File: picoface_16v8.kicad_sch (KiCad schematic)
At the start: 23 parts, among them J1 ZX_Spectrum_Connector_48K_SOR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, J2 DE9_Plug, Q1 DMG2305, SW1 SW_USER, SW2 SW_RESET, SW3 SW_RUN, U2 Pico, U3 74LS240

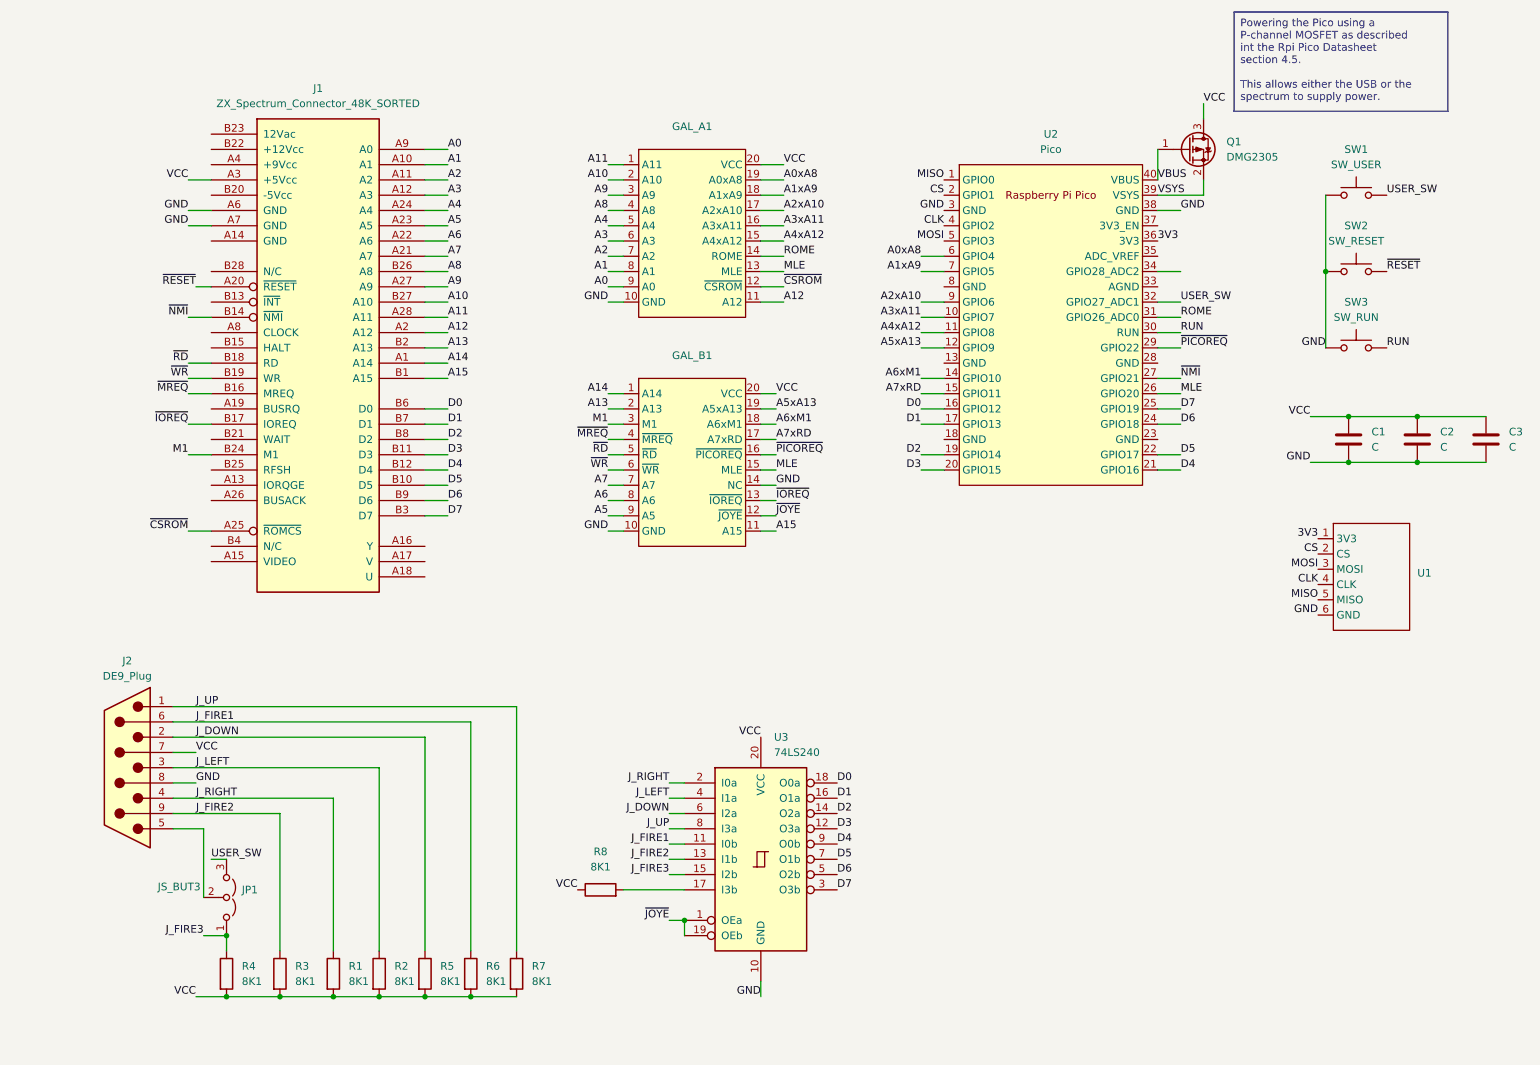
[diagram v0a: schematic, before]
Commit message: Correct resistor typo and add GALASM to schematic
I just blindly typed in 8K1 whereas the resistor I have are 8K2.
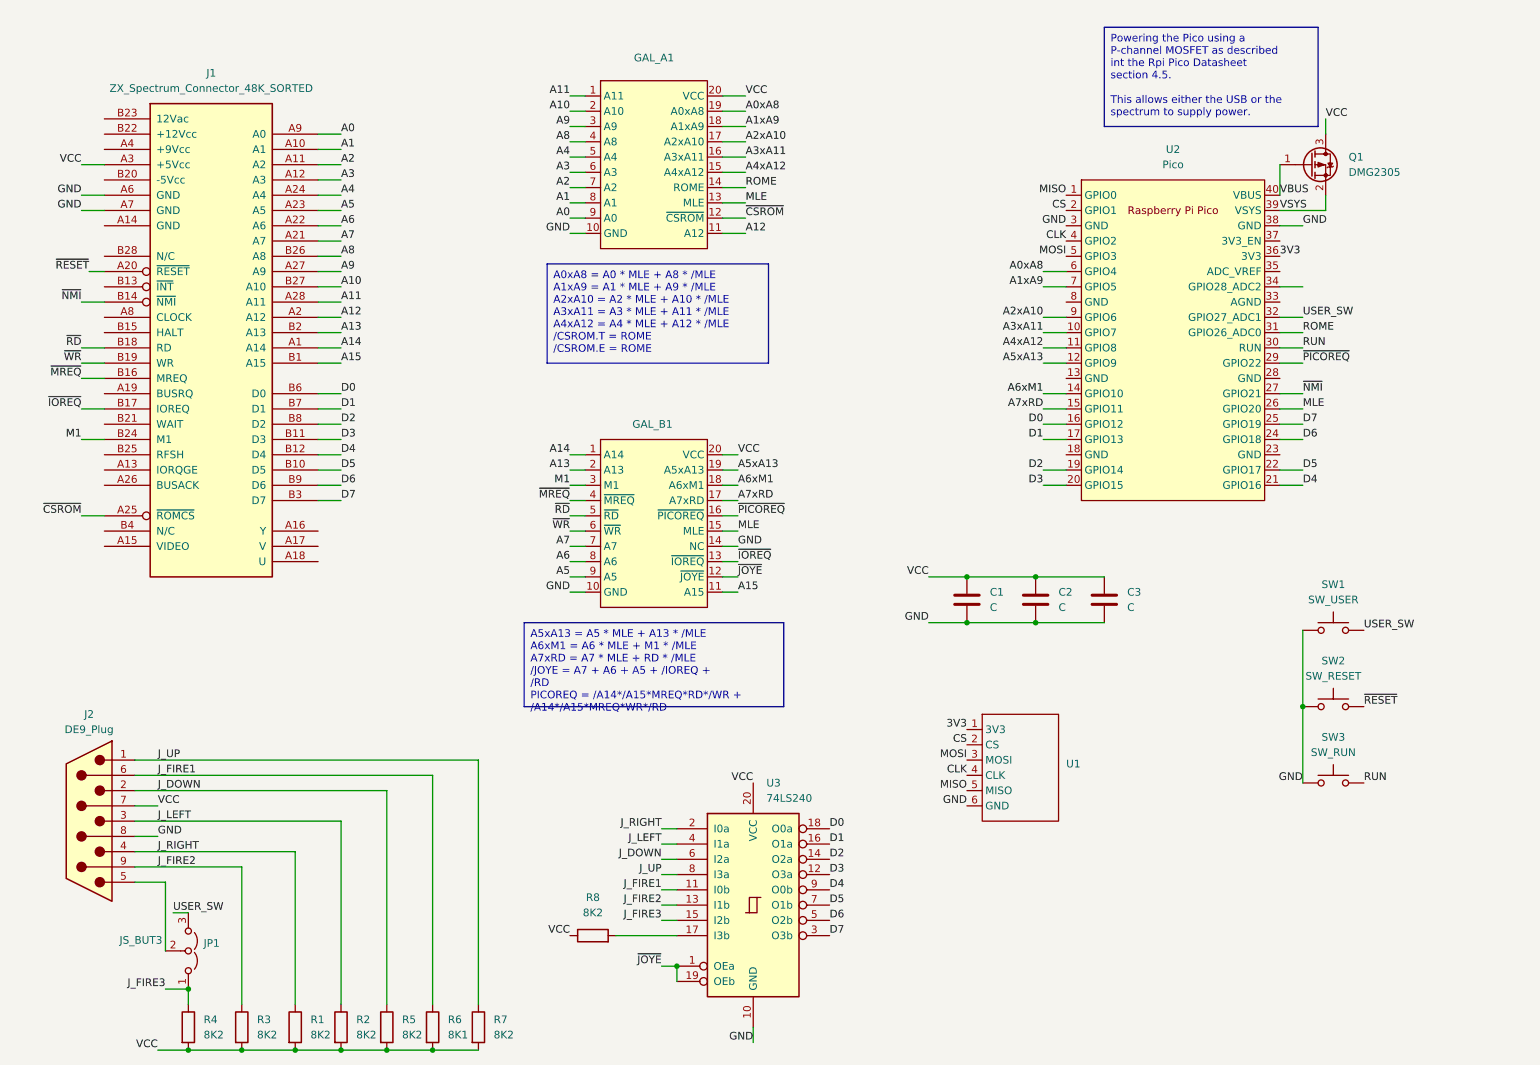
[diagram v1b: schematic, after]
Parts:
- R1, R2, R3, R4, R5, R7, R8: value 8K1 -> 8K2
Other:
- moved on the sheet: C1, C2, C3, GAL_A1, GAL_B1, J1, J2, JP1, Q1, R1, R2, R3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
